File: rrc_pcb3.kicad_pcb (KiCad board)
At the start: 2 copper layers, 138.4 x 68.2 mm, 15 parts, among them J1 Conn_01x02_Male-Connector, J2 Conn_01x03_Male-Connector, J3 digital logic connection, U1 RFD900+, U2 Teensy4.1, U3 BN220-GPS, U4 ICM-20948, U5 MS5611, U6 logo, U7 Conn_01x02_Male-Connector

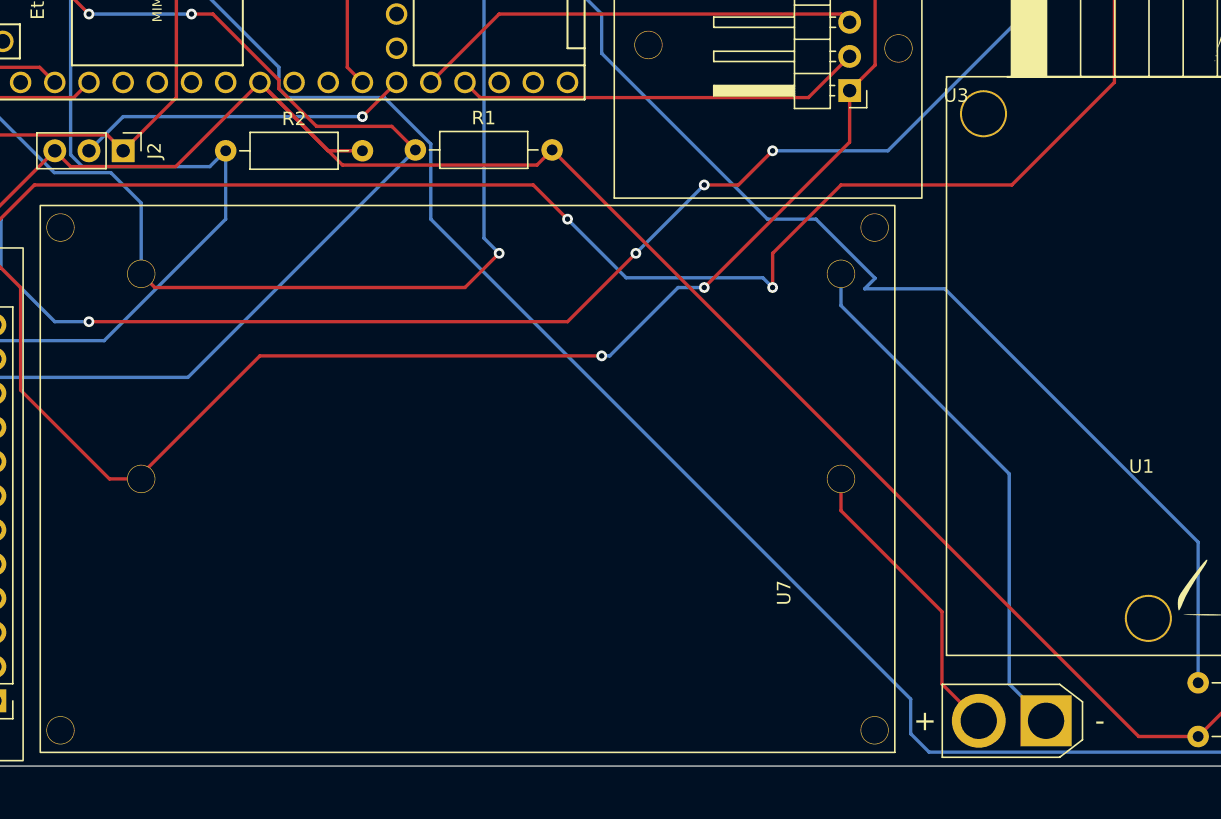
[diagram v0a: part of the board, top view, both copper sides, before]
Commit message: R1&R2 removed
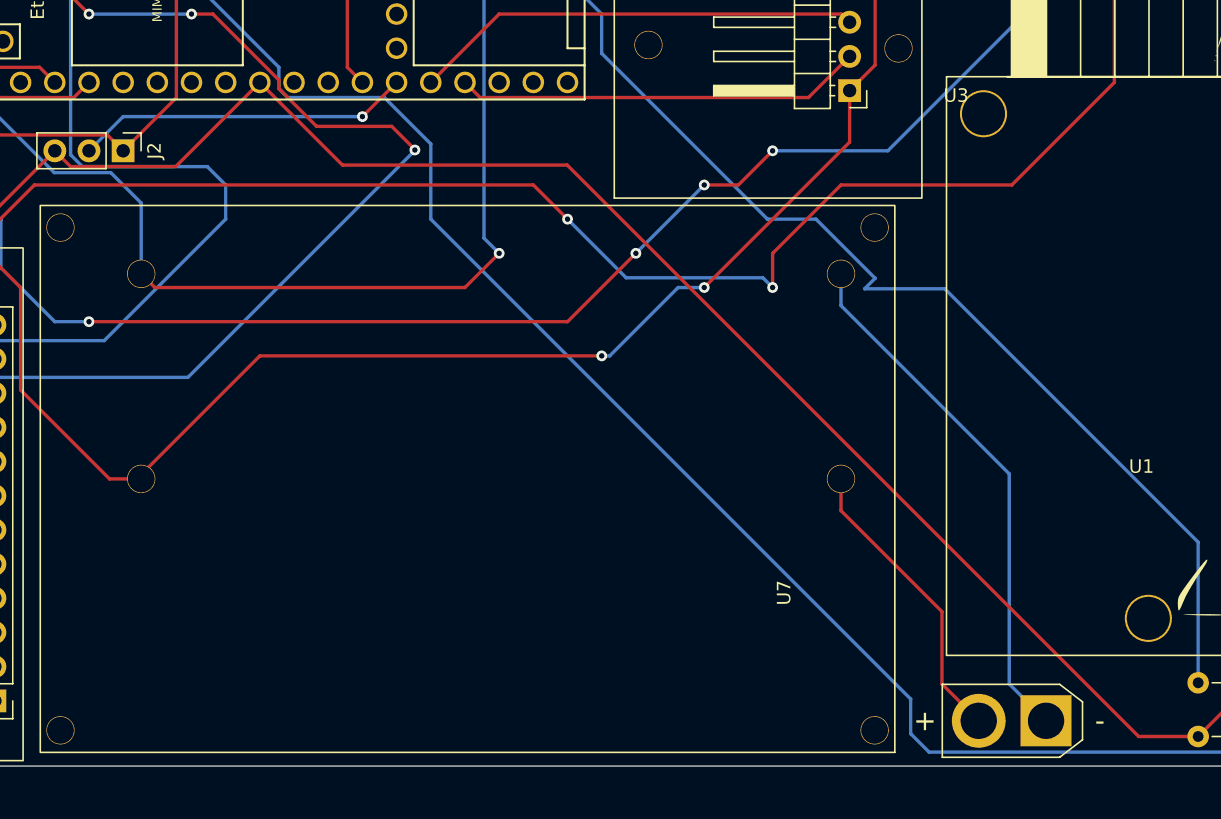
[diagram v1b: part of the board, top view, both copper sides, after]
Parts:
- removed R1, R2: R-Device, Resistor_THT:R_Axial_DIN0207_L6.3mm_D2.5mm_P10.16mm_Horizontal
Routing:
- net T_VCC: track 181.1 -> 170.5 mm
- net SDA: track 64.7 -> 62.2 mm
- net SCL: vias 4 -> 5
